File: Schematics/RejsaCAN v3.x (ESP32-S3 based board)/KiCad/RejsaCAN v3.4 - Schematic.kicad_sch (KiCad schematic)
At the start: 80 parts, among them J1 Micro-Fit 3.0 4P R/A, J2 U.FL, Q1 SS8050, U1 ESP32-S3-WROOM-1(N16R8), U2 SN65HVD230DR, U3 ME2807A33M3G, U4 LMR14010ADDCR, U5 MT9700, U6 GAQY212GS, U7 LG290P03AAMD

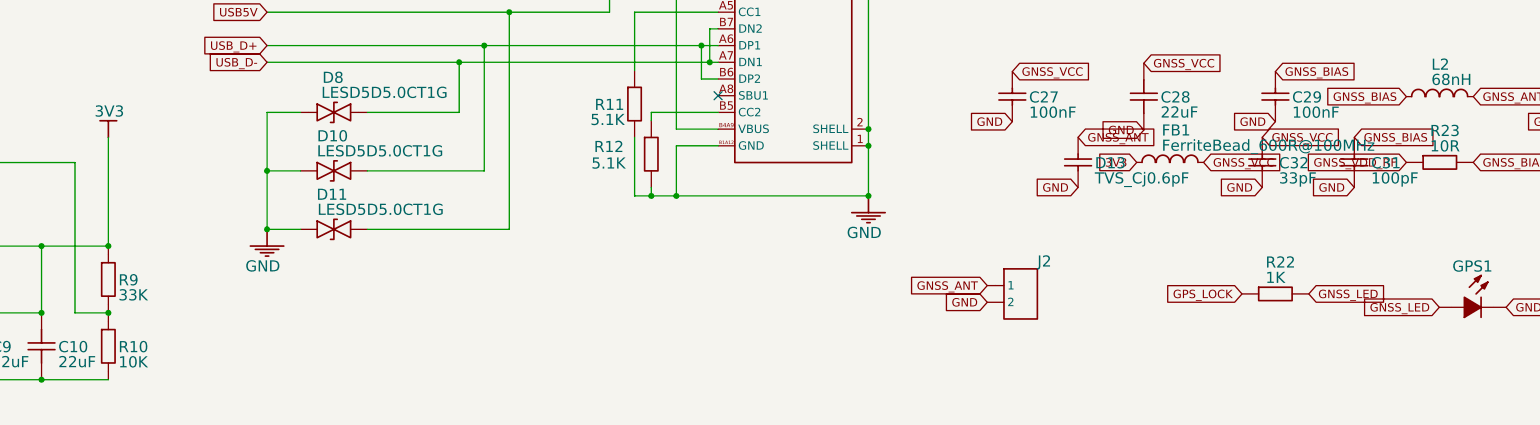
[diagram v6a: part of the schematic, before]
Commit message: Dedicated LDO for the GNSS, and an L-shaped bump-out instead of a wide board
Two changes asked for: give the GNSS its own regulator, and stop
widening the whole board just to fit the module.

LDO
---
FB1's ferrite pi filter is gone; U8 (AP2112K-3.3, SOT-23-5, 600 mA)
now feeds GNSS_VCC from 3V3, EN tied high, with C33 1uF on the input.
This satisfies Quectel's "do not use a switching DC-DC converter",
which the ferrite only softened.

It does not work as a straight drop-in, though, and that is the part
worth recording: the buck was set to 3.29 V and the module wants 3.3 V,
so any 3.3 V LDO fed from it would sit in dropout, where PSRR collapses
and the LDO filters nothing at all. So R9 goes 33k -> 34.8k, raising
3V3 to 0.765 x (1 + 34.8/10) = 3.427 V. That leaves 127 mV of headroom
against ~56 mV of AP2112K dropout at the module's 135 mA peak.

3.427 V is inside the recommended range of everything else on the rail
(ESP32-S3 and SN65HVD230 both 3.0-3.6 V, microSD 2.7-3.6 V, MT9700 to
5.5 V), and it lifts the GAQY212GS drive through R20 390R to 5.6 mA,
still inside its 5-30 mA window.

Outline
-------
The driver is that U1's WROOM antenna keep-out reaches x=149.9, which
is 8.4 mm past the original board edge, so the GNSS has to sit out
there no matter what. Only the module needs to, though.

The board is now L-shaped: main body 110..148, plus a bump-out
148..173 x 194..229.53 carrying U7, the RF chain, J2, the LDO and J1.
2770 mm2 of copper against 3120 mm2 if the full height had been
widened to the same reach.

The bump is on the *bottom* right deliberately. The WROOM's PCB antenna
is at the top edge, so dropping the GNSS low takes the separation from
~35 mm to ~47 mm for free.

RF_IN to J2 is 3.89 mm of 50R run, with J2 5.53 mm from the edge.

DRC
---
All electrical errors are clear: no shorts, no clearance violations, no
board-edge violations. Three were found and fixed in the process --
C30 pad 1 shorting U7 pad 12, C28 pad 1 at 0.015 mm from C33, and J1's
CAN pads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
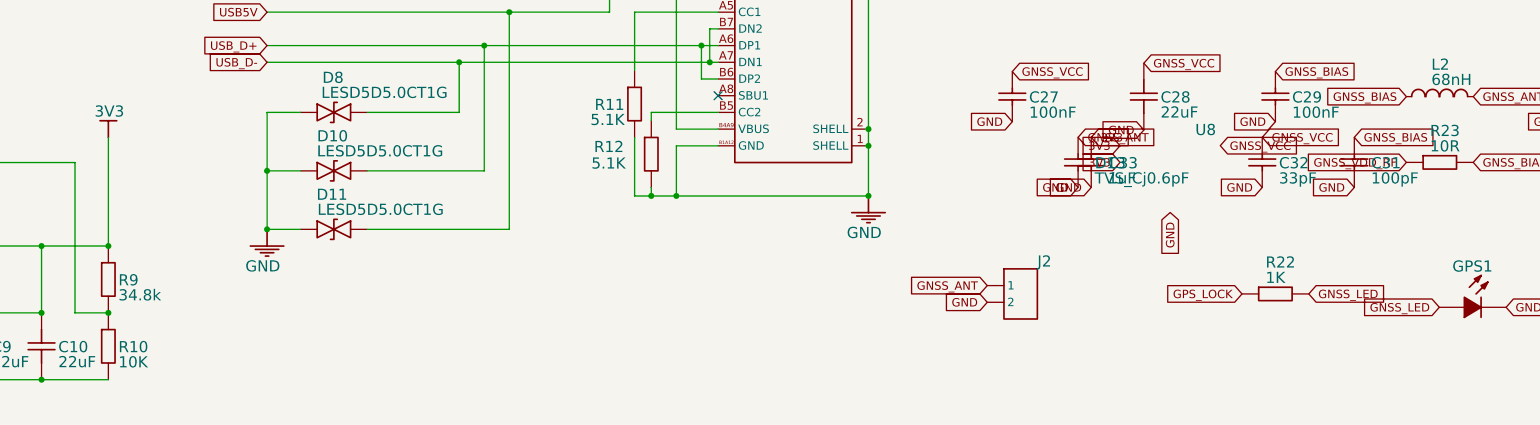
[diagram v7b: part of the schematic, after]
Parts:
- removed FB1: FerriteBead_600R@100MHz, Inductor_SMD:L_0402_1005Metric, symbol SLP6028S100MTT
- added C33: 1uF, Capacitor_SMD:C_0402_1005Metric, symbol CL05B104KO5NNNC_1
- added U8: AP2112K-3.3, Package_TO_SOT_SMD:SOT-23-5, symbol AP2112K-3.3
- R9: value 33K -> 34.8k
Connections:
- net 3V3: now also C33.2
- net GND: now also C33.1
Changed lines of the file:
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@@
 			)
 		)
-		(property "Value" "33K"
+		(property "Value" "34.8k"
 			(at 164.084 179.2097 0)
 			(show_name no)
@@
 	)
 	(symbol
-		(lib_id "SLP6028S100MTT")
-		(at 324 160 0)
+		(lib_id "CL05B104KO5NNNC_1")
+		(at 310 160 0)
 		(unit 0)
 		(body_style 0)
@@
 		(in_pos_files yes)
 		(dnp no)
-		(property "Reference" "FB1"
-			(at 322.705 154.145 0)
+		(property "Reference" "D13"
+			(at 312.54 159.124 0)
 			(show_name no)
 			(do_not_autoplace no)
@@
 			)
 		)
-		(property "Value" "FerriteBead_600R@100MHz"
-			(at 322.705 156.457 0)
+		(property "Value" "TVS_Cj0.6pF"
+			(at 312.54 161.435 0)
 			(show_name no)
 			(do_not_autoplace no)
@@
 			)
 		)
-		(property "Footprint" "Inductor_SMD:L_0402_1005Metric"
-			(at 324 160 0)
+		(property "Footprint" "Diode_SMD:D_0402_1005Metric"
+			(at 310 160 0)
 			(hide yes)
 			(show_name no)
@@
 		)
 		(property "Datasheet" ""
-			(at 324 160 0)
+			(at 310 160 0)
 			(hide yes)
 			(show_name no)
@@
 		)
 		(property "Description" ""
+			(at 310 160 0)
+			(hide yes)
+			(show_name no)
+			(do_not_autoplace no)
+			(effects
+				(font
+					(size 1.27 1.27)
+				)
+			)
+		)
+		(property "Manufacturer Part" "CL05B104KO5NNNC"
+			(at 310 160 0)
+			(hide yes)
+			(show_name no)
+			(do_not_autoplace no)
+			(effects
+				(font
+					(size 1.27 1.27)
+				)
+			)
+		)
+		(property "Manufacturer" "SAMSUNG"
+			(at 310 160 0)
+			(hide yes)
+			(show_name no)
+			(do_not_autoplace no)
+			(effects
+				(font
+					(size 1.27 1.27)
+				)
+			)
+		)
+		(property "Supplier Part" ""
+			(at 310 160 0)
+			(hide yes)
+			(show_name no)
+			(do_not_autoplace no)
+			(effects
+				(font
+					(size 1.27 1.27)
+				)
+			)
+		)
+		(property "Supplier" "LCSC"
+			(at 310 160 0)
+			(hide yes)
+			(show_name no)
+			(do_not_autoplace no)
+			(effects
+				(font
+					(size 1.27 1.27)
+				)
+			)
+		)
+		(pin "2"
+		)
+		(pin "1"
+		)
+		(instances
+			(project "RejsaCAN v3.4 - Schematic"
+				(path "/16c2f03a-5652-4050-b62b-75ebc6e5d249"
+					(reference "D13")
+					(unit 0)
+				)
+			)
+		)
+	)
+	(global_label "GND"
+		(shape input)
+		(at 310 163.81 180)
+		(effects
+			(font
+				(size 1.27 1.27)
+			)
+			(justify right)
+		)
+		(property "Intersheetrefs" "${INTERSHEET_REFS}"
+			(at 310 163.81 0)
+			(hide yes)
+			(show_name no)
+			(do_not_autoplace no)
+			(effects
+				(font
+					(size 1.27 1.27)
+				)
+			)
+		)
+	)
+	(global_label "GNSS_ANT"
+		(shape input)
+		(at 310 156.19 0)
+		(effects
+			(font
+				(size 1.27 1.27)
+			)
+			(justify left)
+		)
+		(property "Intersheetrefs" "${INTERSHEET_REFS}"
+			(at 310 156.19 0)
+			(hide yes)
+			(show_name no)
+			(do_not_autoplace no)
+			(effects
+				(font
+					(size 1.27 1.27)
+				)
+			)
+		)
+	)
+	(symbol
+		(lib_id "AP2112K-3.3")
+		(at 324 160 0)
+		(unit 0)
+		(body_style 0)
+		(exclude_from_sim no)
+		(in_bom yes)
+		(on_board yes)
+		(in_pos_files yes)
+		(dnp no)
+		(property "Reference" "U8"
+			(at 327.81 154.069 0)
+			(show_name no)
+			(do_not_autoplace no)
+			(effects
+				(font
+					(face "Arial")
+					(size 1.6891 1.6891)
+				)
+				(justify left top)
+			)
+		)
+		(property "Value" "AP2112K-3.3"
+			(at 321.231 151.199 0)
+			(hide yes)
+			(show_name no)
+			(do_not_autoplace no)
+			(effects
+				(font
+					(face "Arial")
+					(size 1.6891 1.6891)
+				)
+				(justify left top)
+			)
+		)
+		(property "Footprint" "Package_TO_SOT_SMD:SOT-23-5"
 			(at 324 160 0)
 			(hide yes)
@@
 			)
 		)
-		(property "Manufacturer Part" "SLP6028S100MTT"
+		(property "Datasheet" ""
 			(at 324 160 0)
 			(hide yes)
@@
 			)
 		)
-		(property "Manufacturer" "Sunltech Tech"
+		(property "Description" ""
 			(at 324 160 0)
 			(hide yes)
@@
 		(pin "2"
 		)
+		(pin "3"
+		)
+		(pin "4"
+		)
+		(pin "5"
+		)
 		(instances
 			(project "RejsaCAN v3.4 - Schematic"
 				(path "/16c2f03a-5652-4050-b62b-75ebc6e5d249"
-					(reference "FB1")
+					(reference "U8")
 					(unit 0)
 				)
@@
 	(global_label "3V3"
 		(shape input)
-		(at 318.92 160 180)
+		(at 316.38 157.46 180)
+		(effects
+			(font
+				(size 1.27 1.27)
+			)
+			(justify right)
+		)
+		(property "Intersheetrefs" "${INTERSHEET_REFS}"
+			(at 316.38 157.46 0)
+			(hide yes)
+			(show_name no)
+			(do_not_autoplace no)
+			(effects
+				(font
+					(size 1.27 1.27)
+				)
+			)
+		)
+	)
+	(global_label "GND"
+		(shape input)
+		(at 324 167.62 270)
+		(effects
+			(font
+				(size 1.27 1.27)
+			)
+			(justify right)
+		)
+		(property "Intersheetrefs" "${INTERSHEET_REFS}"
+			(at 324 167.62 0)
+			(hide yes)
+			(show_name no)
+			(do_not_autoplace no)
+			(effects
+				(font
+					(size 1.27 1.27)
+				)
+			)
+		)
+	)
+	(global_label "3V3"
+		(shape input)
+		(at 316.38 160 180)
 		(effects
 			(font
@@
 		)
 		(property "Intersheetrefs" "${INTERSHEET_REFS}"
-			(at 318.92 160 0)
+			(at 316.38 160 0)
 			(hide yes)
 			(show_name no)
@@
 	(global_label "GNSS_VCC"
 		(shape input)
-		(at 329.08 160 0)
+		(at 331.62 157.46 0)
 		(effects
 			(font
@@
 		)
 		(property "Intersheetrefs" "${INTERSHEET_REFS}"
-			(at 329.08 160 0)
+			(at 331.62 157.46 0)
 			(hide yes)
 			(show_name no)
@@
 	(symbol
 		(lib_id "CL05B104KO5NNNC_1")
-		(at 310 160 0)
+		(at 312 160 0)
 		(unit 0)
 		(body_style 0)
@@
 		(in_pos_files yes)
 		(dnp no)
-		(property "Reference" "D13"
-			(at 312.54 159.124 0)
+		(property "Reference" "C33"
+			(at 314.54 159.124 0)
 			(show_name no)
 			(do_not_autoplace no)
@@
 			)
 		)
-		(property "Value" "TVS_Cj0.6pF"
-			(at 312.54 161.435 0)
+		(property "Value" "1uF"
+			(at 314.54 161.435 0)
 			(show_name no)
 			(do_not_autoplace no)
@@
 			)
 		)
-		(property "Footprint" "Diode_SMD:D_0402_1005Metric"
-			(at 310 160 0)
+		(property "Footprint" "Capacitor_SMD:C_0402_1005Metric"
+			(at 312 160 0)
 			(hide yes)
 			(show_name no)
@@
 		)
 		(property "Datasheet" ""
-			(at 310 160 0)
+			(at 312 160 0)
 			(hide yes)
 			(show_name no)
@@
 		)
 		(property "Description" ""
-			(at 310 160 0)
+			(at 312 160 0)
 			(hide yes)
 			(show_name no)
@@
 		)
 		(property "Manufacturer Part" "CL05B104KO5NNNC"
-			(at 310 160 0)
+			(at 312 160 0)
 			(hide yes)
 			(show_name no)
@@
 		)
 		(property "Manufacturer" "SAMSUNG"
-			(at 310 160 0)
+			(at 312 160 0)
 			(hide yes)
 			(show_name no)
@@
 		)
 		(property "Supplier Part" ""
-			(at 310 160 0)
+			(at 312 160 0)
 			(hide yes)
 			(show_name no)
@@
 		)
 		(property "Supplier" "LCSC"
-			(at 310 160 0)
+			(at 312 160 0)
 			(hide yes)
 			(show_name no)
@@
 			(project "RejsaCAN v3.4 - Schematic"
 				(path "/16c2f03a-5652-4050-b62b-75ebc6e5d249"
-					(reference "D13")
+					(reference "C33")
 					(unit 0)
 				)
@@
 	(global_label "GND"
 		(shape input)
-		(at 310 163.81 180)
+		(at 312 163.81 180)
 		(effects
 			(font
@@
 		)
 		(property "Intersheetrefs" "${INTERSHEET_REFS}"
-			(at 310 163.81 0)
+			(at 312 163.81 0)
 			(hide yes)
 			(show_name no)
@@
 		)
 	)
-	(global_label "GNSS_ANT"
+	(global_label "3V3"
 		(shape input)
-		(at 310 156.19 0)
+		(at 312 156.19 0)
 		(effects
 			(font
@@
 		)
 		(property "Intersheetrefs" "${INTERSHEET_REFS}"
-			(at 310 156.19 0)
+			(at 312 156.19 0)
 			(hide yes)
 			(show_name no)

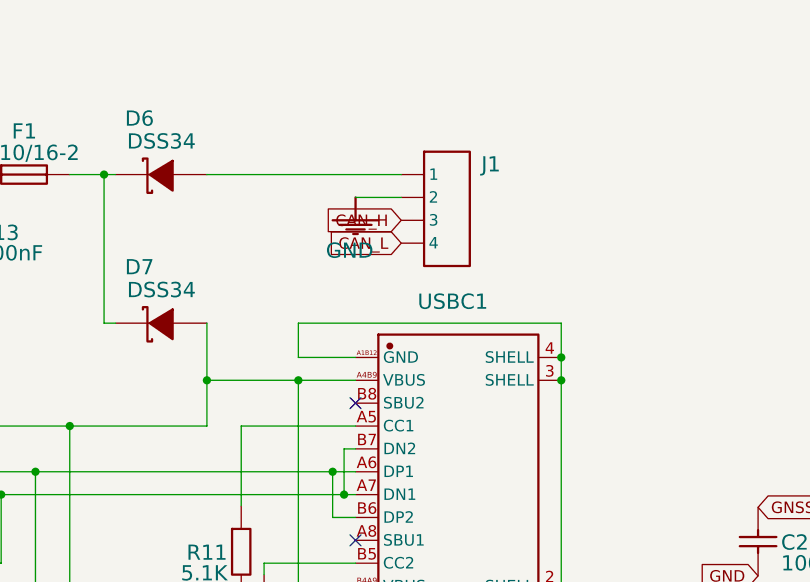
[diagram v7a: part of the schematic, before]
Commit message: Add J3, the LTE breakout: raw 12V, GND, USB_D- and USB_D+
The LTE module talks to the ESP32 over USB rather than UART, so J3
parallels the native USB pair and splits the input 12V off to feed the
module.

  J3.1  VBAT_IN   raw 12V, tapped at J1.1 ahead of D6 and F1
  J3.2  GND
  J3.3  USB_D-    GPIO19
  J3.4  USB_D+    GPIO20

The raw input net was unnamed (Net-(D6-A)); it is now VBAT_IN, carrying
J1.1, J3.1 and D6's anode.

J3 is a JST-XH 4-pin, deliberately NOT another Micro-Fit. Two identical
4-circuit Micro-Fits on one board invite plugging the CAN harness into
the USB port, which would put 12V and CAN_H directly onto USB_D+/- and
GPIO19/20. A different connector family makes that mechanically
impossible. It is also less than half the footprint area (13.49 x 6.84
vs 11.25 x 13.76), which is what let it fit at all.

Both USB lines already carry ESD diodes on the net (D8, D10), so the
new connector inherits that protection with nothing added.

Only one USB port may be connected at a time -- the ESP32-S3 is a USB
device on USBC1 and a USB host to the LTE module, and those cannot
coexist on one D+/D- pair. This is understood and accepted: the module
gets unplugged to program the board. At full speed (12 Mbps, all the
ESP32-S3 OTG supports) the unused branch is a short enough stub not to
matter.

12V for the module is tapped ahead of D6 and F1 on purpose, so the
slave does not consume this board's 1.1A fuse budget and does not push
current through a 3A Schottky. THE SLAVE MUST PROVIDE ITS OWN FUSE AND
REVERSE-POLARITY PROTECTION -- it is fed unprotected battery voltage.

Board: the bump-out grew from y=194 to y=186 to hold J3. With that the
L-shape saves 2970 vs 3120 mm2, only ~5% against a full rectangle --
the cut corner is now mostly what is left of the saving.

DRC: zero electrical and zero outline errors. What remains is 35
courtyard overlaps, 12 holes-inside-courtyard and 4 items-not-allowed,
all pre-existing classes or the GNSS decoupling that Quectel requires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
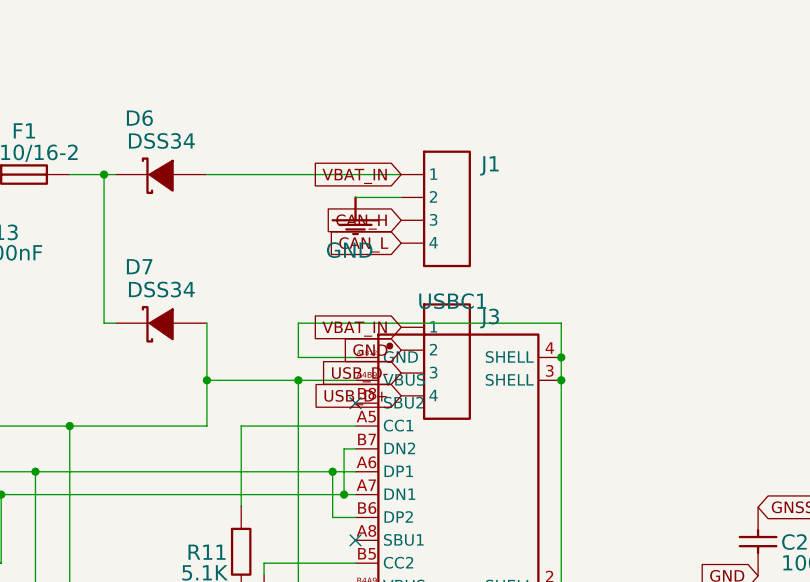
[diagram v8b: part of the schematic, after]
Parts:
- added J3: JST-XH 4P LTE, Connector_JST:JST_XH_B4B-XH-A_1x04_P2.50mm_Vertical, symbol HDR-M-2.54_1x4_1
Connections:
- net GND: now also J3.2
- net USB_D+: now also J3.4
- net USB_D-: now also J3.3
- net VBAT_IN: now reaches D6.2 (A), J1.1
- net VBAT_IN: now also J3.1
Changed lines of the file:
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@@
+		)
+	)
+	(global_label "VBAT_IN"
+		(shape input)
+		(at 260.35 109.22 180)
+		(effects
+			(font
+				(size 1.27 1.27)
+			)
+			(justify right)
+		)
+		(property "Intersheetrefs" "${INTERSHEET_REFS}"
+			(at 260.35 109.22 0)
+			(hide yes)
+			(show_name no)
+			(do_not_autoplace no)
+			(effects
+				(font
+					(size 1.27 1.27)
+				)
+			)
+		)
+	)
+	(symbol
+		(lib_id "HDR-M-2.54_1x4_1")
+		(at 265.43 130 0)
+		(unit 0)
+		(body_style 0)
+		(exclude_from_sim no)
+		(in_bom yes)
+		(on_board yes)
+		(in_pos_files yes)
+		(dnp no)
+		(property "Reference" "J3"
+			(at 269.24 124.069 0)
+			(show_name no)
+			(do_not_autoplace no)
+			(effects
+				(font
+					(face "Arial")
+					(size 1.6891 1.6891)
+				)
+				(justify left top)
+			)
+		)
+		(property "Value" "JST-XH 4P LTE"
+			(at 262.661 121.199 0)
+			(hide yes)
+			(show_name no)
+			(do_not_autoplace no)
+			(effects
+				(font
+					(face "Arial")
+					(size 1.6891 1.6891)
+				)
+				(justify left top)
+			)
+		)
+		(property "Footprint" "Connector_JST:JST_XH_B4B-XH-A_1x04_P2.50mm_Vertical"
+			(at 265.43 130 0)
+			(hide yes)
+			(show_name no)
+			(do_not_autoplace no)
+			(effects
+				(font
+					(size 1.27 1.27)
+				)
+			)
+		)
+		(property "Datasheet" ""
+			(at 265.43 130 0)
+			(hide yes)
+			(show_name no)
+			(do_not_autoplace no)
+			(effects
+				(font
+					(size 1.27 1.27)
+				)
+			)
+		)
+		(property "Description" ""
+			(at 265.43 130 0)
+			(hide yes)
+			(show_name no)
+			(do_not_autoplace no)
+			(effects
+				(font
+					(size 1.27 1.27)
+				)
+			)
+		)
+		(property "Supplier Part" ""
+			(at 265.43 130 0)
+			(hide yes)
+			(show_name no)
+			(do_not_autoplace no)
+			(effects
+				(font
+					(size 1.27 1.27)
+				)
+			)
+		)
+		(property "Supplier" "LCSC"
+			(at 265.43 130 0)
+			(hide yes)
+			(show_name no)
+			(do_not_autoplace no)
+			(effects
+				(font
+					(size 1.27 1.27)
+				)
+			)
+		)
+		(pin "1"
+		)
+		(pin "2"
+		)
+		(pin "3"
+		)
+		(pin "4"
+		)
+		(instances
+			(project "RejsaCAN v3.4 - Schematic"
+				(path "/16c2f03a-5652-4050-b62b-75ebc6e5d249"
+					(reference "J3")
+					(unit 0)
+				)
+			)
+		)
+	)
+	(global_label "VBAT_IN"
+		(shape input)
+		(at 260.35 126.19 180)
+		(effects
+			(font
+				(size 1.27 1.27)
+			)
+			(justify right)
+		)
+		(property "Intersheetrefs" "${INTERSHEET_REFS}"
+			(at 260.35 126.19 0)
+			(hide yes)
+			(show_name no)
+			(do_not_autoplace no)
+			(effects
+				(font
+					(size 1.27 1.27)
+				)
+			)
+		)
+	)
+	(global_label "GND"
+		(shape input)
+		(at 260.35 128.73 180)
+		(effects
+			(font
+				(size 1.27 1.27)
+			)
+			(justify right)
+		)
+		(property "Intersheetrefs" "${INTERSHEET_REFS}"
+			(at 260.35 128.73 0)
+			(hide yes)
+			(show_name no)
+			(do_not_autoplace no)
+			(effects
+				(font
+					(size 1.27 1.27)
+				)
+			)
+		)
+	)
+	(global_label "USB_D-"
+		(shape input)
+		(at 260.35 131.27 180)
+		(effects
+			(font
+				(size 1.27 1.27)
+			)
+			(justify right)
+		)
+		(property "Intersheetrefs" "${INTERSHEET_REFS}"
+			(at 260.35 131.27 0)
+			(hide yes)
+			(show_name no)
+			(do_not_autoplace no)
+			(effects
+				(font
+					(size 1.27 1.27)
+				)
+			)
+		)
+	)
+	(global_label "USB_D+"
+		(shape input)
+		(at 260.35 133.81 180)
+		(effects
+			(font
+				(size 1.27 1.27)
+			)
+			(justify right)
+		)
+		(property "Intersheetrefs" "${INTERSHEET_REFS}"
+			(at 260.35 133.81 0)
+			(hide yes)
+			(show_name no)
+			(do_not_autoplace no)
+			(effects
+				(font
+					(size 1.27 1.27)
+				)
+			)
 		)
 	)
